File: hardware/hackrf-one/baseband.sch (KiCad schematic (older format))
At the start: 101 parts, among them P10 TXBBI, P11 RXBBI, P12 RXBBQ, P14 XCVR_CLKOUT, P15 INTR, P16 CLKIN, P18 OEB, P2 CLKOUT, P36 VAA, P37 SCL, P38 SDA, P39 SSP1_SCK, P40 SSP1_MOSI, P41 SSP1_MISO, P9 TXBBQ, Q3 MOSFET_P, T3 RX_BALUN, T4 TX_BALUN, U17 MAX2837, U18 MAX5864, U19 SI5351C, X1 GSG-XTAL4PIN

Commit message: fixed SMA connector selection
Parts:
- P16, P2: Description CONN JACK SMA PCB VERT -> CONN SMA JACK 50 OHM EDGE MNT; Manufacturer TE Connectivity -> Linx Technologies; Part Number 2081233-1 -> CONSMA003.062
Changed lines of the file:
@@
 F 2 "" H 5500 9600 60  0001 C CNN
 F 3 "" H 5500 9600 60  0001 C CNN
-F 4 "TE Connectivity" H 5500 9600 60  0001 C CNN "Manufacturer"
-F 5 "2081233-1" H 5500 9600 60  0001 C CNN "Part Number"
-F 6 "CONN JACK SMA PCB VERT" H 5500 9600 60  0001 C CNN "Description"
+F 4 "Linx Technologies" H 5500 9600 60  0001 C CNN "Manufacturer"
+F 5 "CONSMA003.062" H 5500 9600 60  0001 C CNN "Part Number"
+F 6 "CONN SMA JACK 50 OHM EDGE MNT" H 5500 9600 60  0001 C CNN "Description"
 	1    5500 9600
 	-1   0    0    -1
@@
 F 2 "" H 3500 8850 60  0001 C CNN
 F 3 "" H 3500 8850 60  0001 C CNN
-F 4 "TE Connectivity" H 3500 8850 60  0001 C CNN "Manufacturer"
-F 5 "2081233-1" H 3500 8850 60  0001 C CNN "Part Number"
-F 6 "CONN JACK SMA PCB VERT" H 3500 8850 60  0001 C CNN "Description"
+F 4 "Linx Technologies" H 3500 8850 60  0001 C CNN "Manufacturer"
+F 5 "CONSMA003.062" H 3500 8850 60  0001 C CNN "Part Number"
+F 6 "CONN SMA JACK 50 OHM EDGE MNT" H 3500 8850 60  0001 C CNN "Description"
 	1    3500 8850
 	1    0    0    -1

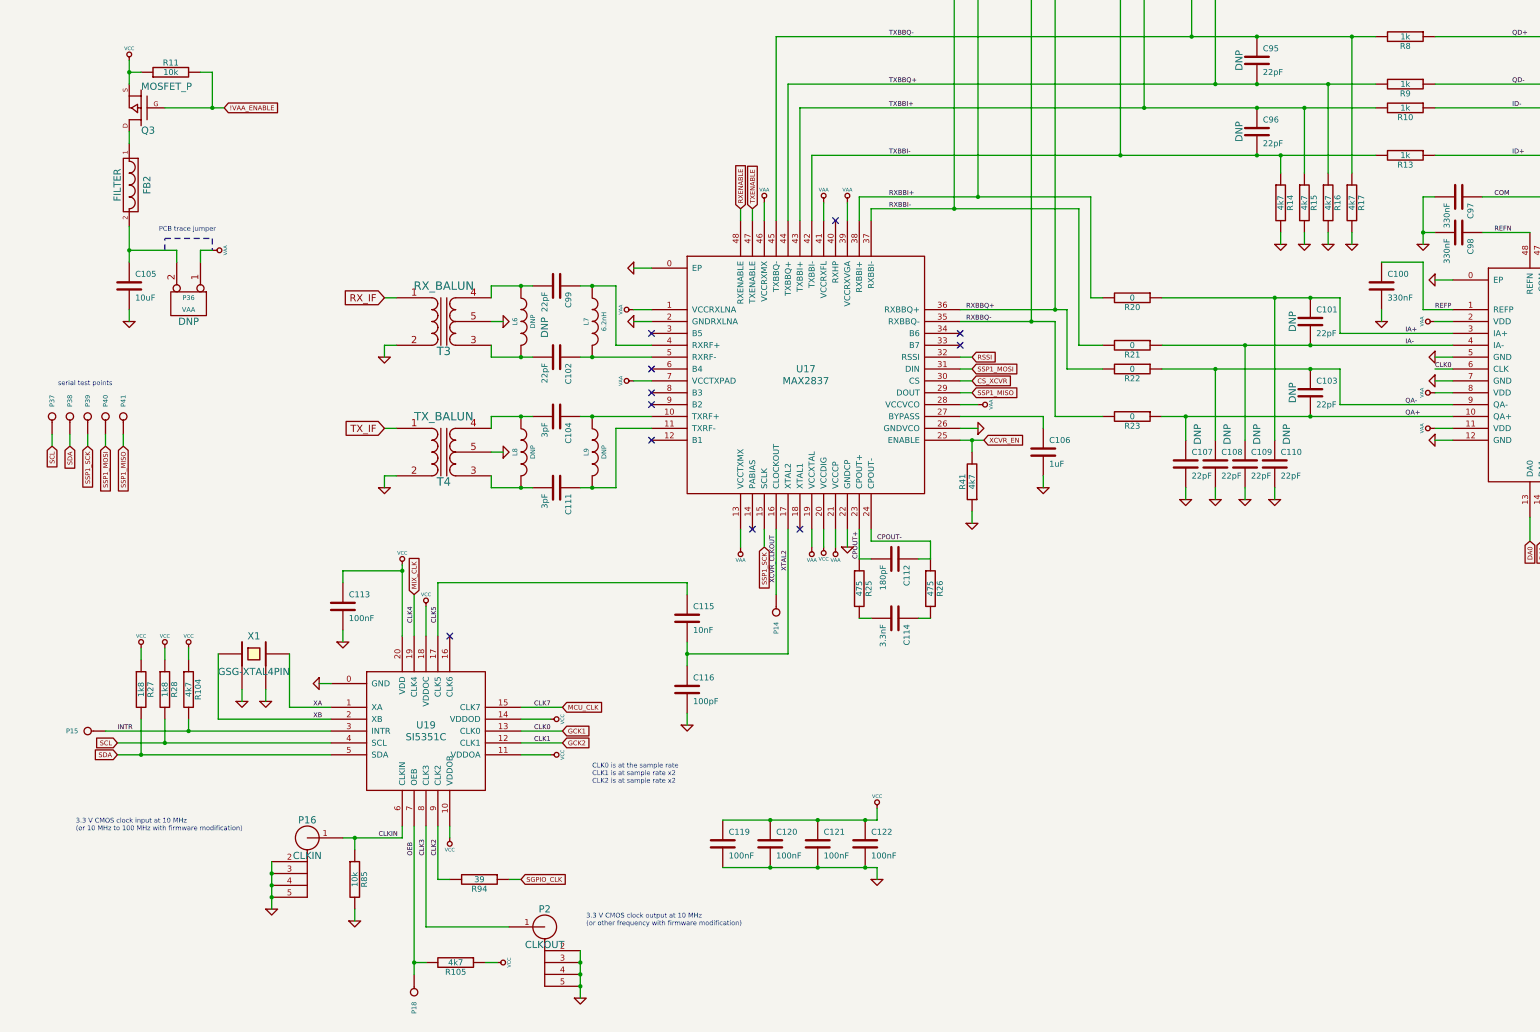
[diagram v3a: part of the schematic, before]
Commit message: extra footprints for clock signal passives just in case
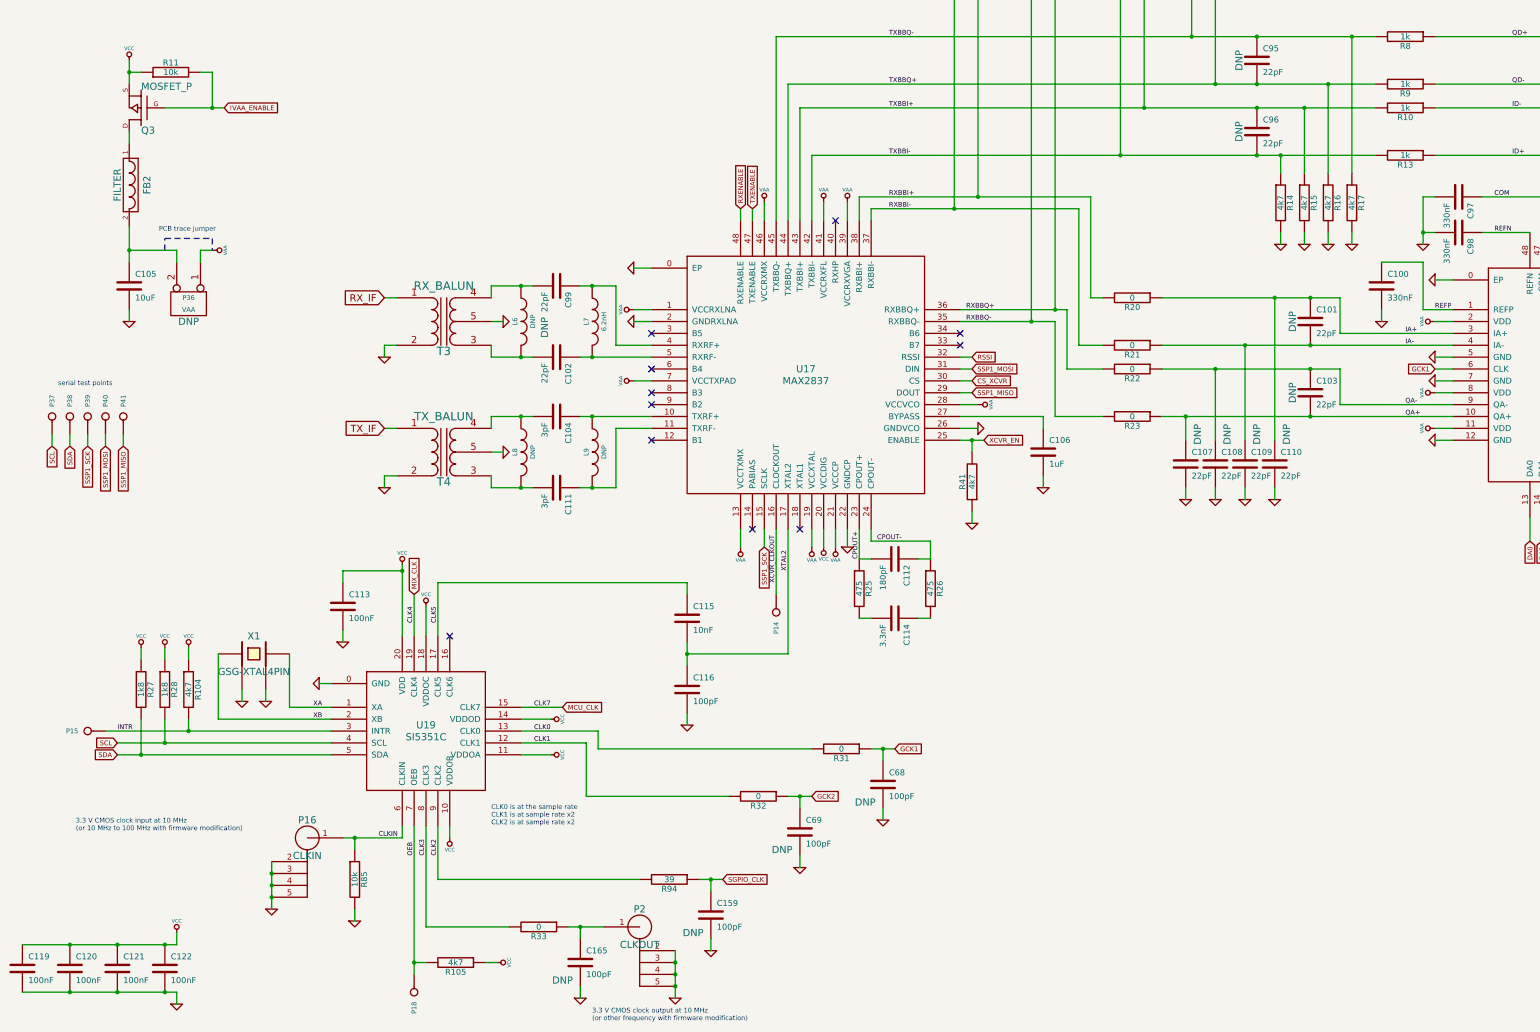
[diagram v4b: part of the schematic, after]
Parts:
- added C159, C165, C68, C69: 100pF, symbol C
- added R31, R32, R33: 0, symbol R
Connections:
- net CLK3: now also R33.2; no longer P2.1 (RF)
- net GCK1: now also C68.1, R31.1; no longer U19.13 (CLK0)
- net GCK2: now also C69.1, R32.1; no longer U19.12 (CLK1)
- net GND: now also C159.2, C165.2, C68.2, C69.2
- net SGPIO_CLK: now also C159.1
- new net: C165.1, P2.1 (RF), R33.1
- new net CLK0: R31.2, U19.13 (CLK0)
- new net CLK1: R32.2, U19.12 (CLK1)
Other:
- moved on the sheet: C119, C120, C121, C122, P2, R94

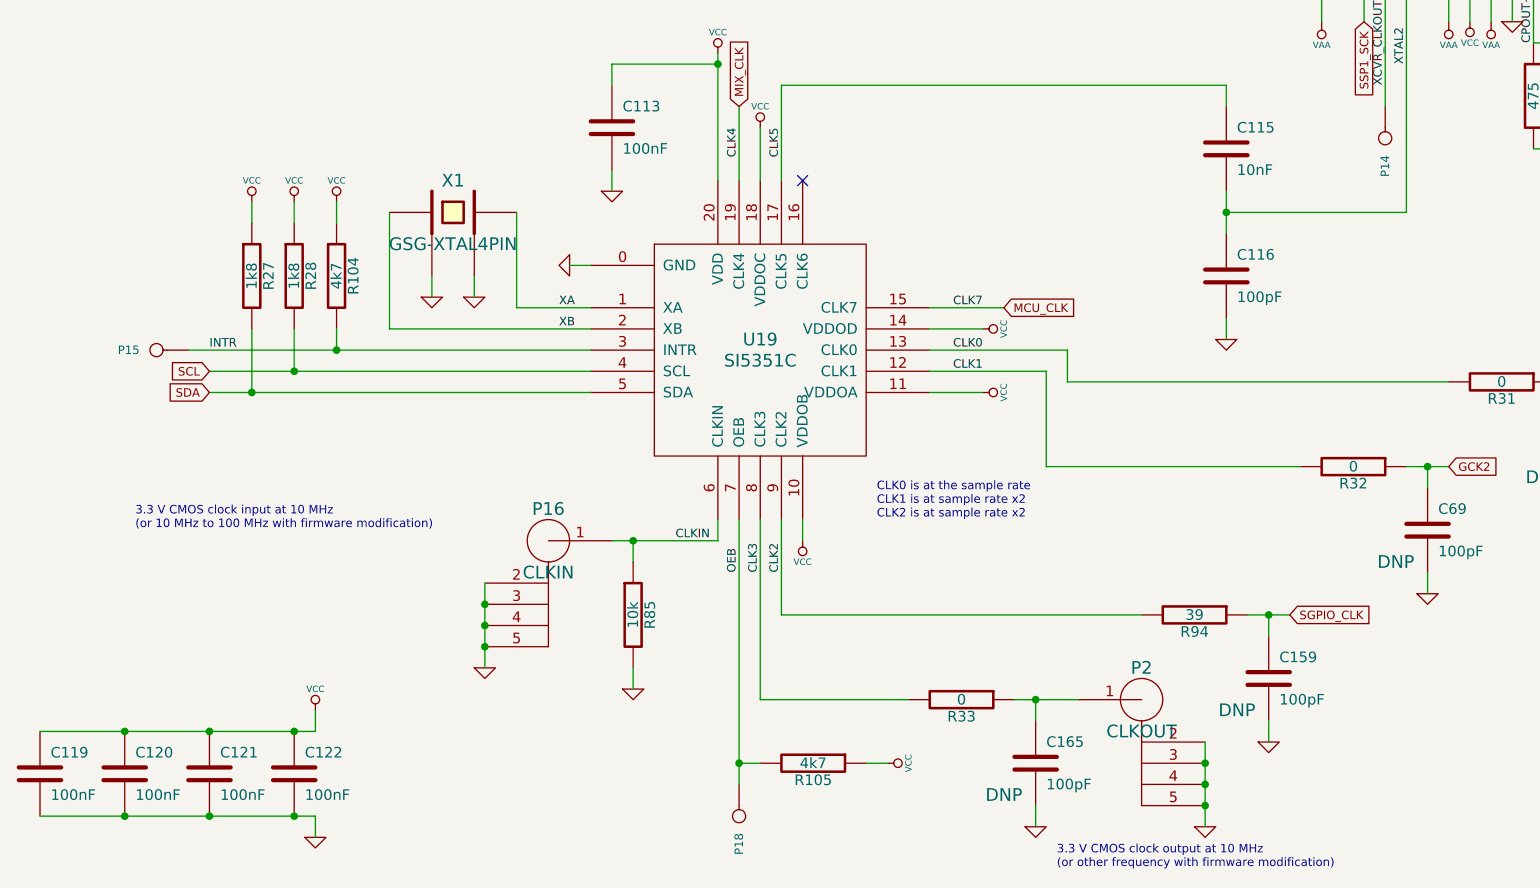
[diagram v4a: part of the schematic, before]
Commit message: P22 consolidation, expansion
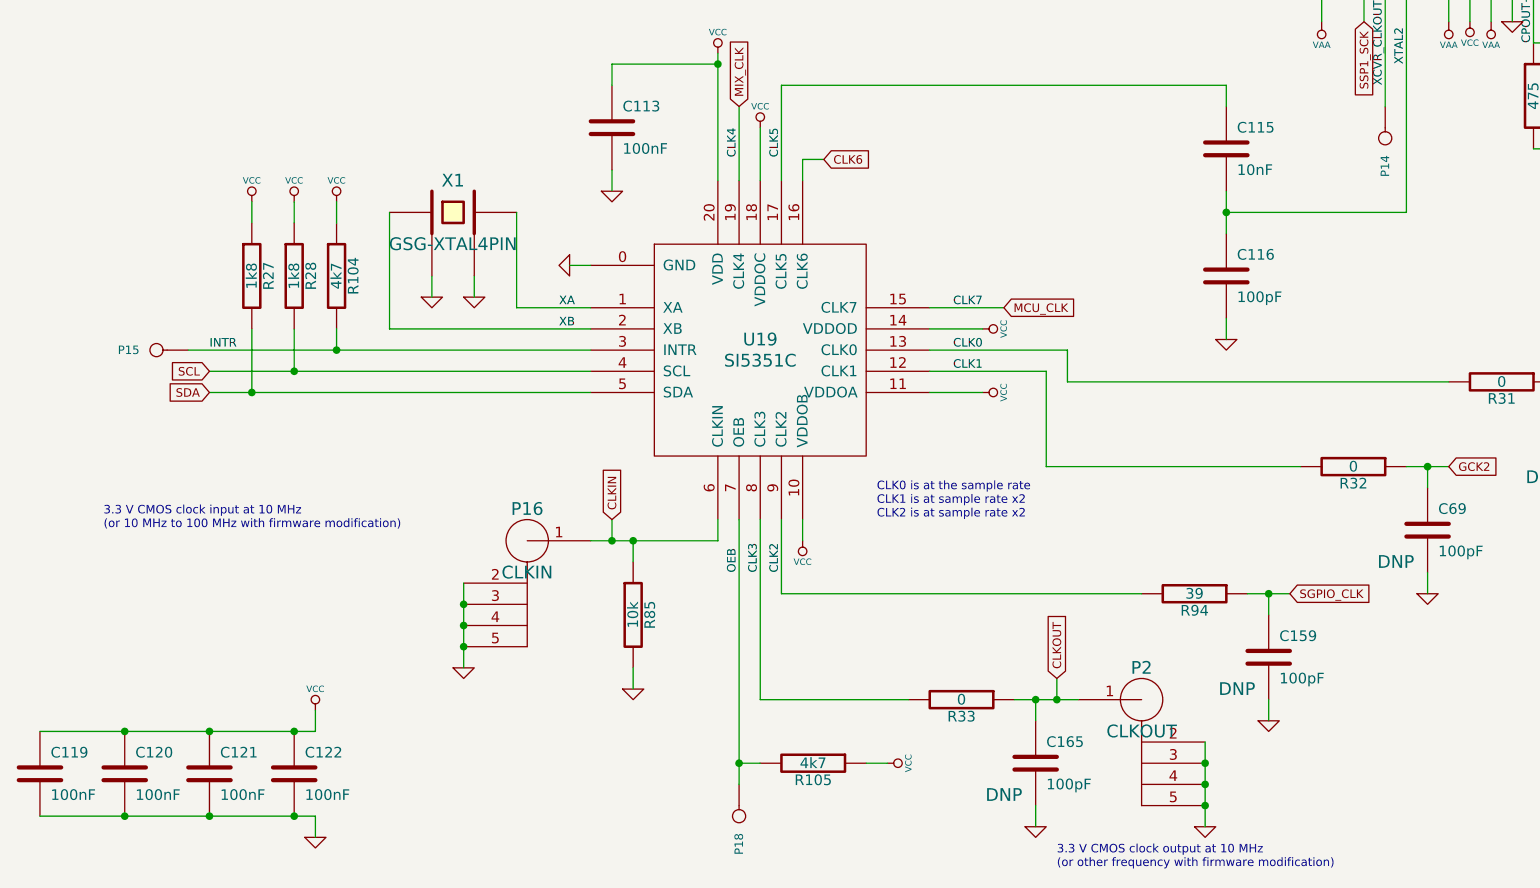
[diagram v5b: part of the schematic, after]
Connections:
- net CLK6: now reaches U19.16 (CLK6)
- net CLKOUT: now reaches C165.1, P2.1 (RF), R33.1
- no-connect marks 11 -> 10
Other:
- moved on the sheet: C159, P16, R94
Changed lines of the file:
@@
 Text Notes 5900 10400 0    40   ~ 0
 3.3 V CMOS clock output at 10 MHz\n(or other frequency with firmware modification)
-Text Notes 1550 8800 0    40   ~ 0
+Text Notes 1400 8800 0    40   ~ 0
 3.3 V CMOS clock input at 10 MHz\n(or 10 MHz to 100 MHz with firmware modification)
 $Comp
@@
 	1    0    0    -1
 $EndComp
-NoConn ~ 4700 7150
 $Comp
 L GSG-SMA-CONN P2
@@
 	1    0    0    -1
 $EndComp
-Text GLabel 7000 9200 2    40   Input ~ 0
+Text GLabel 7000 9100 2    40   Input ~ 0
 SGPIO_CLK
 Text Notes 5050 8750 0    40   ~ 0
@@
 	0    1    1    0
 $EndComp
-Text Label 4100 8850 0    40   ~ 0
-CLKIN
 Text Label 3550 7850 0    40   ~ 0
 XB
@@
 L GND #PWR0115
 U 1 1 4F5D1728
-P 3200 9450
-F 0 "#PWR0115" H 3200 9450 30  0001 C CNN
-F 1 "GND" H 3200 9380 30  0001 C CNN
-F 2 "" H 3200 9450 60  0001 C CNN
-F 3 "" H 3200 9450 60  0001 C CNN
-	1    3200 9450
+P 3100 9450
+F 0 "#PWR0115" H 3100 9450 30  0001 C CNN
+F 1 "GND" H 3100 9380 30  0001 C CNN
+F 2 "" H 3100 9450 60  0001 C CNN
+F 3 "" H 3100 9450 60  0001 C CNN
+	1    3100 9450
 	1    0    0    -1
 $EndComp
@@
 L GSG-SMA-CONN P16
 U 1 1 4F5D16D6
-P 3500 8850
-F 0 "P16" H 3500 9000 60  0000 C CNN
-F 1 "CLKIN" H 3500 8700 60  0000 C CNN
-F 2 "" H 3500 8850 60  0001 C CNN
-F 3 "" H 3500 8850 60  0001 C CNN
-F 4 "Linx Technologies" H 3500 8850 60  0001 C CNN "Manufacturer"
-F 5 "CONSMA003.062" H 3500 8850 60  0001 C CNN "Part Number"
-F 6 "CONN SMA JACK 50 OHM EDGE MNT" H 3500 8850 60  0001 C CNN "Description"
-	1    3500 8850
+P 3400 8850
+F 0 "P16" H 3400 9000 60  0000 C CNN
+F 1 "CLKIN" H 3400 8700 60  0000 C CNN
+F 2 "" H 3400 8850 60  0001 C CNN
+F 3 "" H 3400 8850 60  0001 C CNN
+F 4 "Linx Technologies" H 3400 8850 60  0001 C CNN "Manufacturer"
+F 5 "CONSMA003.062" H 3400 8850 60  0001 C CNN "Part Number"
+F 6 "CONN SMA JACK 50 OHM EDGE MNT" H 3400 8850 60  0001 C CNN "Description"
+	1    3400 8850
 	1    0    0    -1
 $EndComp
@@
 L R R94
 U 1 1 50C136DB
-P 6550 9200
-F 0 "R94" V 6630 9200 50  0000 C CNN
-F 1 "39" V 6550 9200 50  0000 C CNN
-F 2 "" H 6550 9200 60  0001 C CNN
-F 3 "" H 6550 9200 60  0001 C CNN
-F 4 "Stackpole" H 6550 9200 60  0001 C CNN "Manufacturer"
-F 5 "RMCF0402JT39R0" H 6550 9200 60  0001 C CNN "Part Number"
-F 6 "RES 39 OHM 1/16W 5% 0402 SMD" H 6550 9200 60  0001 C CNN "Description"
-	1    6550 9200
+P 6550 9100
+F 0 "R94" V 6630 9100 50  0000 C CNN
+F 1 "39" V 6550 9100 50  0000 C CNN
+F 2 "" H 6550 9100 60  0001 C CNN
+F 3 "" H 6550 9100 60  0001 C CNN
+F 4 "Stackpole" H 6550 9100 60  0001 C CNN "Manufacturer"
+F 5 "RMCF0402JT39R0" H 6550 9100 60  0001 C CNN "Part Number"
+F 6 "RES 39 OHM 1/16W 5% 0402 SMD" H 6550 9100 60  0001 C CNN "Description"
+	1    6550 9100
 	0    1    1    0
 $EndComp
@@
 	15200 7800 15200 7700
 Wire Wire Line
-	4600 9200 6300 9200
+	4600 9100 6300 9100
 Wire Wire Line
 	1800 5450 1800 5550
@@
 Wire Wire Line
 	14200 3750 14200 2700
-Connection ~ 3200 9150
+Connection ~ 3100 9150
 Wire Wire Line
 	7550 6250 7550 7300
@@
 Wire Wire Line
 	4500 9900 4400 9900
-Connection ~ 3200 9250
+Connection ~ 3100 9250
 Wire Wire Line
 	3150 7600 3150 7700
@@
 Wire Wire Line
 	2950 7700 2950 7600
-Connection ~ 3200 9350
+Connection ~ 3100 9350
 Wire Wire Line
-	3200 9050 3200 9450
+	3100 9050 3100 9450
 Wire Wire Line
 	5000 9900 5100 9900
@@
 	6700 7200 6700 7400
 Wire Wire Line
-	4600 9200 4600 8750
+	4600 9100 4600 8750
 Wire Wire Line
 	6600 9800 6600 10200
@@
 	3900 9450 3900 9550
 Wire Wire Line
-	3800 8850 4300 8850
+	3700 8850 4300 8850
 Wire Wire Line
 	10950 2100 10950 1500
@@
 L C C159
 U 1 1 527F2F05
-P 6900 9500
-F 0 "C159" H 6950 9600 50  0000 L CNN
-F 1 "100pF" H 6950 9400 50  0000 L CNN
-F 2 "" H 6900 9500 60  0001 C CNN
-F 3 "" H 6900 9500 60  0001 C CNN
-F 4 "Murata" H 6900 9500 60  0001 C CNN "Manufacturer"
-F 5 "GRM1555C1H101JZ01D" H 6900 9500 60  0001 C CNN "Part Number"
-F 6 "CAP CER 100PF 50V 5% NP0 0402" H 6900 9500 60  0001 C CNN "Description"
-F 7 "DNP" H 6750 9350 60  0000 C CNN "Note"
-	1    6900 9500
+P 6900 9400
+F 0 "C159" H 6950 9500 50  0000 L CNN
+F 1 "100pF" H 6950 9300 50  0000 L CNN
+F 2 "" H 6900 9400 60  0001 C CNN
+F 3 "" H 6900 9400 60  0001 C CNN
+F 4 "Murata" H 6900 9400 60  0001 C CNN "Manufacturer"
+F 5 "GRM1555C1H101JZ01D" H 6900 9400 60  0001 C CNN "Part Number"
+F 6 "CAP CER 100PF 50V 5% NP0 0402" H 6900 9400 60  0001 C CNN "Description"
+F 7 "DNP" H 6750 9250 60  0000 C CNN "Note"
+	1    6900 9400
 	1    0    0    -1
 $EndComp
 Wire Wire Line
-	6800 9200 7000 9200
+	6800 9100 7000 9100
 Wire Wire Line
-	6900 9200 6900 9300
-Connection ~ 6900 9200
+	6900 9100 6900 9200
+Connection ~ 6900 9100
 $Comp
 L GND #PWR0158
 U 1 1 527F2F0F
-P 6900 9800
-F 0 "#PWR0158" H 6900 9800 30  0001 C CNN
-F 1 "GND" H 6900 9730 30  0001 C CNN
-F 2 "" H 6900 9800 60  0000 C CNN
-F 3 "" H 6900 9800 60  0000 C CNN
-	1    6900 9800
+P 6900 9700
+F 0 "#PWR0158" H 6900 9700 30  0001 C CNN
+F 1 "GND" H 6900 9630 30  0001 C CNN
+F 2 "" H 6900 9700 60  0000 C CNN
+F 3 "" H 6900 9700 60  0000 C CNN
+	1    6900 9700
 	1    0    0    -1
 $EndComp
 Wire Wire Line
-	6900 9700 6900 9800
+	6900 9600 6900 9700
 $Comp
 L R R33
@@
 Text GLabel 13000 4900 0    40   Input ~ 0
 GCK1
+Wire Wire Line
+	5900 9500 5900 9600
+Connection ~ 5900 9600
+Text GLabel 5900 9500 1    40   Input ~ 0
+CLKOUT
+Wire Wire Line
+	3800 8850 3800 8750
+Connection ~ 3800 8850
+Text GLabel 3800 8750 1    40   Input ~ 0
+CLKIN
+Wire Wire Line
+	4700 7150 4700 7050
+Text GLabel 4800 7050 2    40   Input ~ 0
+CLK6
+Wire Wire Line
+	4700 7050 4800 7050
 $EndSCHEMATC

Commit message: many test points
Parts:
- added P53: CS_XCVR, symbol CONN_1
- added P54: CS_AD, symbol CONN_1
- added P55: TXENABLE, symbol CONN_1
- added P56: RXENABLE, symbol CONN_1
- added P57: XTAL2, symbol CONN_1
- added P58: GCK1, symbol CONN_1
- added P59: GCK2, symbol CONN_1
- added P60: SGPIO_CLK, symbol CONN_1
- added P61: DA0, symbol CONN_1
- added P62: DA7, symbol CONN_1
- added P63: DD0, symbol CONN_1
- added P64: DD9, symbol CONN_1
- added P65: DA4, symbol CONN_1
- added P66: DD5, symbol CONN_1
- added P67: RSSI, symbol CONN_1
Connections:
- net CS_AD: now also P54.1
- net CS_XCVR: now also P53.1
- net DA0: now also P61.1
- net DA4: now also P65.1
- net DA7: now also P62.1
- net DD0: now also P63.1
- net DD5: now also P66.1
- net DD9: now also P64.1
- net GCK1: now also P58.1
- net GCK2: now also P59.1
- net RSSI: now also P67.1
- net RXENABLE: now also P56.1
- net SGPIO_CLK: now also P60.1
- net TXENABLE: now also P55.1
- net XTAL2: now also P57.1
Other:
- note added: "test points"
- note removed: "serial test points"
- moved on the sheet: P37, P38, P39, P40, P41
